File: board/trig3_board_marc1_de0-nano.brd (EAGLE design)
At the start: 233.2 x 160 mm, 305 parts, among them IC1 ICL7660CPA, IC2 ICL7660CPA, IC3 ICL7660CPA, IC4 ICL7660CPA, J10 2p-2.54, J11 2p-2.54, J12 4p-2.54, J13 BU-SMB-V, J131 4p-2.54, J14 BU-SMB-V, J141 2p-2.54, J15 2p-2.54, J16 2p-2.54, J17 2p-2.54, J18 2p-2.54, J19 6HE-160-VG64AC, J20 4p-2.54, J21 4p-2.54, J22 2p-2.54, J23 2p-2.54, J24 2p-2.54, J25 2p-2.54, J26 4p-2.54, J27 4p-2.54, J28 2p-2.54, J29 2p-2.54, J3 4p-2.54, J30 2p-2.54, J31 2p-2.54, J311 4p-2.54, J32 2p-2.54, J33 2p-2.54, J34 2p-2.54, J35 2p-2.54, J36 2p-2.54, J37 2p-2.54, J38 2p-2.54, J39 2p-2.54, J4 2p-2.54, J40 2p-2.54, J41 2p-2.54, J42 2p-2.54, J43 2p-2.54, J48 2p-2.54, J49 2p-2.54, J5 2p-2.54, J50 2p-2.54, J51 2p-2.54, J52 2p-2.54, J53 2p-2.54, J54 2p-2.54, J55 2p-2.54, J6 2p-2.54, J7 4p-2.54, J8 2p-2.54, J9 2p-2.54, K15_R10P BU-SMB-V, K16_R10N BU-SMB-V, M16CLK_3N BU-SMB-V, P11 BU-SMB-V, P14_CLKOUT_4P BU-SMB-V, P15 BU-SMB-V, P16_R15N BU-SMB-V, P9 BU-SMB-V, T10_B16N BU-SMB-V, T12_B18N BU-SMB-V, T13_B20N BU-SMB-V, T14_B23P BU-SMB-V, T15_B23N BU-SMB-V, T9CLK_7N BU-SMB-V

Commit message: slim it down and add usb-serial
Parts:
- removed A12_T21N, A14_CLKOUT_2N, A2_T2N, A3_T2P, A5, A7_T9N, A8CLK_4N, B11, B12_T21P, B16, B5, B7_T9P, B8CLK_4P, C11, C14, C15, C16, C3_CLKOUT_3N, C6, C8, C9_T15N, D11, D14, D15, D16, D3_CLKOUT_3P, D5, D6, D8, D9_T15P, E10, E11, E15CLK_2P, E16CLK_2N, E6, E7, E8_T10N, E9, F14, F15, F16, F8_T10P, F9, G15_R5P, G16_R5N, J13, J14, K15_R10P, K16_R10N, L16_R11N, M16CLK_3N, N12, N14, N15_R13P, N16_R13N, P11, P14_CLKOUT_4P, P15, R10_B16P, R12_B18P, R13_B20P, R14_CLKOUT_4N, T10_B16N, T12_B18N, T13_B20N, T14_B23P, T15_B23N: BU-SMB-V, con-coax:BU-SMB-V
- removed C1, C12, C13, C17, C18, C3, C7, C9: 10uF, SparkFun-Capacitors:CAP-PTH-5MM
- removed C19, C2, C20, C21, C22, C4, C5, C91, C93, C94, C95, C97: 0.1uF, SparkFun-Capacitors:0805
- removed IC1, IC2, IC3, IC4: ICL7660CPA, maxim:DIL08
- removed J1, J2: (no value), SparkFun-Connectors:2X13
- removed J10, J11, J141, J15, J16, J17, J18, J22, J23, J24, J25, J28, J29, J30, J31, J32, J33, J35, J36, J37, J38, J39, J4, J40, J41, J48, J49, J50, J51, J52, J53, J54, J55, J8, J9, OJ1, OJ10, OJ11, OJ12, OJ17, OJ18, OJ19, OJ2, OJ20, OJ21, OJ22, OJ23, OJ24, OJ25, OJ26, OJ27, OJ28, OJ29, OJ3, OJ30, OJ31, OJ32, OJ33, OJ34, OJ35, OJ36, OJ37, OJ38, OJ39, OJ4, OJ40, OJ49, OJ5, OJ50, OJ51, OJ52, OJ53, OJ54, OJ55, OJ56, OJ57, OJ58, OJ59, OJ6, OJ60, OJ61, OJ62, OJ63, OJ64, OJ65, OJ66, OJ67, OJ68, OJ69, OJ7, OJ70, OJ71, OJ72, OJ73, OJ74, OJ75, OJ76, OJ77, OJ78, OJ79, OJ8, OJ80, OJ9: 2p-2.54, Seeed-Connector:H2-2.54
- removed J131, J20, J21, J26, J27, J311: 4p-2.54, Seeed-Connector:H4-2.54
- removed J19: 6HE-160-VG64AC, 19inch:6HE_160-VG64AC
- removed R10, R12, R13, R14: 1k, SparkFun-Passives:AXIAL-0.3
- removed R100, R11, R111, R141, R15, R161, R18, R19, R20, R21, R22, R23, R24, R25, R26, R27, R28, R29, R30, R32, R33, R35, R39, R4, R40, R45, R46, R47, R49, R50, R51, R52, R53, R9, R91: 50, SparkFun-Passives:AXIAL-0.3
- removed R17: 10k, SparkFun-Passives:AXIAL-0.3
- removed R2, R3, R7: 3296W 5k, resistor:RTRIM3296W
- removed VSLUE, VSLUE2, VSLUE3, VSLUE4, VSLUE6, VSLUE7, VSLUE8, VSLUE9: SN74ACT244DW, SN74ACT244DW:SOIC127P1030X265-20N
- added C_OSC1, C_OSC2: 22pF, rcl@1:C0603
- added U340G: CH340G, usb-serial:SOIC16
- added USB1: MF-CON-MICROUSB-RIGHT, PP_Connectors:10118193-0001LF
- added Y1: ABL-12.000MHZ-B2, SparkFun-FreqCtrl:HC49US
- R1: value 3296W 5k -> 10k; device resistor:RTRIM3296W -> adafruit:R0805
- moved R1 126.3 mm to (95.0, 98.0)
- moved J3 110.0 mm to (-35.0, 107.0)
- moved B4 89.9 mm to (66.9, 74.0)
- moved C10 89.9 mm to (94.0, 80.0)
- moved D12 89.9 mm to (111.0, 74.0)
- moved OJ89 89.9 mm to (77.9, 68.0)
- moved OJ90 89.9 mm to (68.0, 68.0)
- moved OJ91 89.9 mm to (102.0, 68.0)
- moved OJ92 89.9 mm to (112.1, 68.0)
- moved OJ93 89.9 mm to (78.0, 64.0)
- moved OJ94 89.9 mm to (68.0, 64.0)
- moved OJ95 89.9 mm to (112.0, 64.0)
- moved OJ96 89.9 mm to (102.0, 64.0)
- moved VSLUE11 89.9 mm to (89.0, 71.0)
- moved A4 89.9 mm to (76.9, 74.0)
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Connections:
- removed net -3V3_1: C3.1, IC1.5, J20.1, R10.P$2
- removed net -3V3_2: C9.1, IC2.5, J21.1, R12.P$2
- removed net -3V3_3: C13.1, IC3.5, J26.1, R13.P$2
- removed net -3V3_4: C18.1, IC4.5, J27.1, R14.P$2
- removed net -V1: C19.2, J20.2, OJ9.1, R1.2
- removed net -V2: C20.2, J21.2, OJ10.1, R2.2
- removed net -V3: C21.2, J26.2, OJ11.1, R3.2
- removed net -V4: C22.2, J27.2, OJ12.1, R7.2
- removed net AIN0: J1.24, J131.4
- removed net AIN1: J1.25, J311.1
- removed net AIN2: J1.22, J131.3
- removed net AIN3: J1.21, J311.3
- removed net AIN4: J1.23, J311.2
- removed net AIN5: J1.18, J131.1
- removed net AIN6: J1.19, J311.4
- removed net AIN7: J1.20, J131.2
- removed net GPIO_018_E7: OJ64.1, SV1.23, VSLUE7.6, VSLUE7.8
- removed net GPIO_019_D8: OJ21.1, SV1.24, VSLUE2.15, VSLUE2.17
- removed net GPIO_01_C3: C3_CLKOUT_3N.1, J30.2, R27.P$2, SV1.4
- removed net GPIO_021_F8: F8_T10P.1, J18.2, R21.P$2, SV1.26
- removed net GPIO_022_F9: OJ62.1, SV1.27, VSLUE7.11, VSLUE7.13
- removed net GPIO_023_E9: OJ24.1, SV1.28, VSLUE2.6, VSLUE2.8
- removed net GPIO_112_N12: OJ23.1, SV2.17, VSLUE2.2, VSLUE2.4
- removed net GPIO_120_P15: OJ61.1, SV2.25, VSLUE7.15, VSLUE7.17
- removed net GPIO_20_A14: A14_CLKOUT_2N.1, J1.5, J31.2, R29.P$2
- removed net GPIO_210_F14: J1.15, OJ30.1, VSLUE3.11, VSLUE3.13
- removed net GPIO_211_G16: G16_R5N.1, J1.16, J28.2, R24.P$2
- removed net GPIO_212_G15: G15_R5P.1, J1.17, J29.2, R26.P$2
- removed net GPIO_21_B16: J1.6, OJ22.1, VSLUE2.11, VSLUE2.13
- removed net GPIO_22_C14: J1.7, OJ32.1, VSLUE3.6, VSLUE3.8
- removed net GPIO_23_C16: J1.8, OJ63.1, VSLUE7.2, VSLUE7.4
- removed net GPIO_24_C15: J1.9, OJ31.1, VSLUE3.2, VSLUE3.4
- removed net GPIO_25_D16: J1.10, OJ39.1, VSLUE4.2, VSLUE4.4
- removed net GPIO_26_D15: J1.11, OJ29.1, VSLUE3.15, VSLUE3.17
- removed net GPIO_27_D14: J1.12, OJ40.1, VSLUE4.6, VSLUE4.8
- removed net GPIO_28_F15: J1.13, OJ37.1, VSLUE4.15, VSLUE4.17
- removed net GPIO_29_F16: J1.14, OJ38.1, VSLUE4.11, VSLUE4.13
- removed net GPIO_2_IN0_E15CLK: E15CLK_2P.1, J1.2, J16.2, R19.P$2
- removed net GPIO_2_IN1_E16CLK: E16CLK_2N.1, J1.3, J15.2, R18.P$2
- removed net GPIO_2_IN2_M16CLK: J1.4, J141.2, M16CLK_3N.1, R15.P$2
- removed net N$1: C1.1, IC1.2
- removed net N$10: R1.3, R10.P$1
- removed net N$11: R12.P$1, R2.3
- removed net N$12: R13.P$1, R3.3
- removed net N$13: R14.P$1, R7.3
- removed net N$2: C1.2, IC1.4
- removed net N$3: C12.1, IC3.2
- removed net N$4: C7.1, IC2.2
- removed net N$5: C7.2, IC2.4
- removed net N$6: C12.2, IC3.4
- removed net N$7: C17.1, IC4.2
- removed net N$8: C17.2, IC4.4
- removed net OUT1: J14.1, OJ1.1, VSLUE.16, VSLUE.18
- removed net OUT10: E9.1, OJ19.1, VSLUE2.12, VSLUE2.14
- removed net OUT11: D8.1, OJ17.1, VSLUE2.3, VSLUE2.5
- removed net OUT12: B16.1, OJ18.1, VSLUE2.7, VSLUE2.9
- removed net OUT13: C15.1, OJ28.1, VSLUE3.16, VSLUE3.18
- removed net OUT14: C14.1, OJ27.1, VSLUE3.12, VSLUE3.14
- removed net OUT15: D15.1, OJ25.1, VSLUE3.3, VSLUE3.5
- removed net OUT16: F14.1, OJ26.1, VSLUE3.7, VSLUE3.9
- removed net OUT17: D16.1, OJ36.1, VSLUE4.16, VSLUE4.18
- removed net OUT18: D14.1, OJ35.1, VSLUE4.12, VSLUE4.14
- removed net OUT19: F15.1, OJ33.1, VSLUE4.3, VSLUE4.5
- removed net OUT2: D11.1, OJ2.1, VSLUE.12, VSLUE.14
- removed net OUT20: F16.1, OJ34.1, VSLUE4.7, VSLUE4.9
- removed net OUT25: D6.1, OJ52.1, VSLUE6.16, VSLUE6.18
- removed net OUT26: C6.1, OJ51.1, VSLUE6.12, VSLUE6.14
- removed net OUT27: C8.1, OJ49.1, VSLUE6.3, VSLUE6.5
- removed net OUT28: E6.1, OJ50.1, VSLUE6.7, VSLUE6.9
- removed net OUT29: C16.1, OJ60.1, VSLUE7.16, VSLUE7.18
- removed net OUT3: B11.1, OJ3.1, VSLUE.7, VSLUE.9
- removed net OUT30: E7.1, OJ59.1, VSLUE7.12, VSLUE7.14
- removed net OUT31: OJ57.1, P15.1, VSLUE7.3, VSLUE7.5
- removed net OUT32: F9.1, OJ58.1, VSLUE7.7, VSLUE7.9
- removed net OUT33: B5.1, OJ68.1, VSLUE8.16, VSLUE8.18
- removed net OUT34: A5.1, OJ67.1, VSLUE8.12, VSLUE8.14
- removed net OUT35: D5.1, OJ65.1, VSLUE8.3, VSLUE8.5
- removed net OUT36: N14.1, OJ66.1, VSLUE8.7, VSLUE8.9
- removed net OUT37: E11.1, OJ76.1, VSLUE9.16, VSLUE9.18
- removed net OUT38: OJ75.1, P11.1, VSLUE9.12, VSLUE9.14
- removed net OUT39: J13.1, OJ73.1, VSLUE9.3, VSLUE9.5
- removed net OUT4: E10.1, OJ4.1, VSLUE.3, VSLUE.5
- removed net OUT40: C11.1, OJ74.1, VSLUE9.7, VSLUE9.9
- removed net OUT9: N12.1, OJ20.1, VSLUE2.16, VSLUE2.18
- new net +3V3: U340G.16, U340G.4
- new net DMINUS: U340G.6, USB1.2
- new net DPLUS: U340G.5, USB1.3
- new net N$23: C_OSC1.1, U340G.7, Y1.1
- new net N$31: C_OSC2.1, U340G.8, Y1.2
- new net SLD: USB1.S1, USB1.S2, USB1.S3, USB1.S4
- net 3V3: no longer IC1.8, IC2.8, IC3.8, IC4.8, J1.1, J20.4, J21.4, J26.4, J27.4
- net 5V: now also R1.2, USB1.1; no longer C2.2, C4.2, C5.2, C91.2, C93.2, C94.2, C95.2, C97.2, J19.1-A32, J19.1-C32, J19.2-A32, J19.2-C32, R17.P$1, VSLUE.20, VSLUE2.20, VSLUE3.20, VSLUE4.20, VSLUE6.20, VSLUE7.20, VSLUE8.20, VSLUE9.20
- net GND: now also C_OSC1.2, C_OSC2.2, U340G.1, USB1.5; no longer A12_T21N.2, A12_T21N.3, A12_T21N.4, A12_T21N.5, A14_CLKOUT_2N.2, A14_CLKOUT_2N.3, A14_CLKOUT_2N.4, A14_CLKOUT_2N.5, A2_T2N.2, A2_T2N.3, A2_T2N.4, A2_T2N.5, A3_T2P.2, A3_T2P.3, A3_T2P.4, A3_T2P.5, A5.2, A5.3, A5.4, A5.5, A7_T9N.2, A7_T9N.3, A7_T9N.4, A7_T9N.5, A8CLK_4N.2, A8CLK_4N.3, A8CLK_4N.4, A8CLK_4N.5, B11.2, B11.3, B11.4, B11.5, B12_T21P.2, B12_T21P.3, B12_T21P.4, B12_T21P.5, B16.2, B16.3, B16.4, B16.5, B5.2, B5.3, B5.4, B5.5, B7_T9P.2, B7_T9P.3, B7_T9P.4, B7_T9P.5, B8CLK_4P.2, B8CLK_4P.3, B8CLK_4P.4, B8CLK_4P.5, C11.2, C11.3, C11.4, C11.5, C13.2, C14.2, C14.3, C14.4, C14.5, C15.2, C15.3, C15.4, C15.5, C16.2, C16.3, C16.4, C16.5, C18.2, C19.1, C2.1, C20.1, C21.1, C22.1, C3.2, C3_CLKOUT_3N.2, C3_CLKOUT_3N.3, C3_CLKOUT_3N.4, C3_CLKOUT_3N.5, C4.1, C5.1, C6.2, C6.3, C6.4, C6.5, C8.2, C8.3, C8.4, C8.5, C9.2, C91.1, C93.1, C94.1, C95.1, C97.1, C9_T15N.2, C9_T15N.3, C9_T15N.4, C9_T15N.5, D11.2, D11.3, D11.4, D11.5, D14.2, D14.3, D14.4, D14.5, D15.2, D15.3, D15.4, D15.5, D16.2, D16.3, D16.4, D16.5, D3_CLKOUT_3P.2, D3_CLKOUT_3P.3, D3_CLKOUT_3P.4, D3_CLKOUT_3P.5, D5.2, D5.3, D5.4, D5.5, D6.2, D6.3, D6.4, D6.5, D8.2, D8.3, D8.4, D8.5, D9_T15P.2, D9_T15P.3, D9_T15P.4, D9_T15P.5, E10.2, E10.3, E10.4, E10.5, E11.2, E11.3, E11.4, E11.5, E15CLK_2P.2, E15CLK_2P.3, E15CLK_2P.4, E15CLK_2P.5, E16CLK_2N.2, E16CLK_2N.3, E16CLK_2N.4, E16CLK_2N.5, E6.2, E6.3, E6.4, E6.5, E7.2, E7.3, E7.4, E7.5, E8_T10N.2, E8_T10N.3, E8_T10N.4, E8_T10N.5, E9.2, E9.3, E9.4, E9.5, F14.2, F14.3, F14.4, F14.5, F15.2, F15.3, F15.4, F15.5, F16.2, F16.3, F16.4, F16.5, F8_T10P.2, F8_T10P.3, F8_T10P.4, F8_T10P.5, F9.2, F9.3, F9.4, F9.5, G15_R5P.2, G15_R5P.3, G15_R5P.4, G15_R5P.5, G16_R5N.2, G16_R5N.3, G16_R5N.4, G16_R5N.5, IC1.3, IC2.3, IC3.3, IC4.3, J1.26, J10.1, J11.1, J13.2, J13.3, J13.4, J13.5, J14.2, J14.3, J14.4, J14.5, J141.1, J15.1, J16.1, J17.1, J18.1, J19.1-A9, J19.1-C9, J19.2-A9, J19.2-C9, J20.3, J21.3, J22.1, J23.1, J24.1, J25.1, J26.3, J27.3, J28.1, J29.1, J30.1, J31.1, J32.1, J33.1, J35.1, J36.1, J37.1, J38.1, J39.1, J4.1, J40.1, J41.1, J48.1, J49.1, J50.1, J51.1, J52.1, J53.1, J54.1, J55.1, J8.1, J9.1, K15_R10P.2, K15_R10P.3, K15_R10P.4, K15_R10P.5, K16_R10N.2, K16_R10N.3, K16_R10N.4, K16_R10N.5, L16_R11N.2, L16_R11N.3, L16_R11N.4, L16_R11N.5, M16CLK_3N.2, M16CLK_3N.3, M16CLK_3N.4, M16CLK_3N.5, N12.2, N12.3, N12.4, N12.5, N14.2, N14.3, N14.4, N14.5, N15_R13P.2, N15_R13P.3, N15_R13P.4, N15_R13P.5, N16_R13N.2, N16_R13N.3, N16_R13N.4, N16_R13N.5, OJ1.2, OJ17.2, OJ18.2, OJ19.2, OJ2.2, OJ20.2, OJ21.2, OJ22.2, OJ23.2, OJ24.2, OJ25.2, OJ26.2, OJ27.2, OJ28.2, OJ29.2, OJ3.2, OJ30.2, OJ31.2, OJ32.2, OJ33.2, OJ34.2, OJ35.2, OJ36.2, OJ37.2, OJ38.2, OJ39.2, OJ4.2, OJ40.2, OJ49.2, OJ5.2, OJ50.2, OJ51.2, OJ52.2, OJ53.2, OJ54.2, OJ55.2, OJ56.2, OJ57.2, OJ58.2, OJ59.2, OJ6.2, OJ60.2, OJ61.2, OJ62.2, OJ63.2, OJ64.2, OJ65.2, OJ66.2, OJ67.2, OJ68.2, OJ69.2, OJ7.2, OJ70.2, OJ71.2, OJ72.2, OJ73.2, OJ74.2, OJ75.2, OJ76.2, OJ77.2, OJ78.2, OJ79.2, OJ8.2, OJ80.2, P11.2, P11.3, P11.4, P11.5, P14_CLKOUT_4P.2, P14_CLKOUT_4P.3, P14_CLKOUT_4P.4, P14_CLKOUT_4P.5, P15.2, P15.3, P15.4, P15.5, R1.1, R100.P$1, R10_B16P.2, R10_B16P.3, R10_B16P.4, R10_B16P.5, R11.P$1, R111.P$1, R12_B18P.2, R12_B18P.3, R12_B18P.4, R12_B18P.5, R13_B20P.2, R13_B20P.3, R13_B20P.4, R13_B20P.5, R141.P$1, R14_CLKOUT_4N.2, R14_CLKOUT_4N.3, R14_CLKOUT_4N.4, R14_CLKOUT_4N.5, R15.P$1, R161.P$1, R18.P$1, R19.P$1, R2.1, R20.P$1, R21.P$1, R22.P$1, R23.P$1, R24.P$1, R25.P$1, R26.P$1, R27.P$1, R28.P$1, R29.P$1, R3.1, R30.P$1, R32.P$1, R33.P$1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
- net GPIO_00_D3: no longer D3_CLKOUT_3P.1, J50.2, R51.P$2
- net GPIO_012_B7: no longer B7_T9P.1, J49.2, R50.P$2
- net GPIO_013_D6: no longer OJ55.1, VSLUE6.2, VSLUE6.4
- net GPIO_014_A7: no longer A7_T9N.1, J35.2, OJ9.2, R33.P$2
- net GPIO_015_C6: no longer OJ56.1, VSLUE6.6, VSLUE6.8
- net GPIO_016_C8: no longer OJ53.1, VSLUE6.15, VSLUE6.17
- net GPIO_017_E6: no longer OJ54.1, VSLUE6.11, VSLUE6.13
- net GPIO_020_E8: no longer E8_T10N.1, J41.2, OJ12.2, R40.P$2
- net GPIO_024_C9: no longer C9_T15N.1, J8.2, R91.P$2
- net GPIO_025_D9: no longer D9_T15P.1, J11.2, R141.P$2
- net GPIO_026_E11: no longer OJ79.1, VSLUE9.2, VSLUE9.4
- net GPIO_027_E10: no longer OJ5.1, VSLUE.15, VSLUE.17
- net GPIO_028_C11: no longer OJ78.1, VSLUE9.11, VSLUE9.13
- net GPIO_029_B11: no longer OJ6.1, VSLUE.11, VSLUE.13
- net GPIO_02_A2: no longer A2_T2N.1, J22.2, R20.P$2
- net GPIO_030_A12: no longer A12_T21N.1, J36.2, OJ10.2, R9.P$2
- net GPIO_031_D11: no longer OJ8.1, VSLUE.6, VSLUE.8
- net GPIO_033_B12: no longer B12_T21P.1, J37.2, R11.P$2
- net GPIO_03_A3: no longer A3_T2P.1, J25.2, R25.P$2
- net GPIO_07_B5: no longer OJ71.1, VSLUE8.2, VSLUE8.4
- net GPIO_08_A5: no longer OJ72.1, VSLUE8.6, VSLUE8.8
- net GPIO_09_D5: no longer OJ69.1, VSLUE8.15, VSLUE8.17
- net GPIO_0_IN0_A8CLK: no longer A8CLK_4N.1, J24.2, R23.P$2
- net GPIO_0_IN1_B8CLK: no longer B8CLK_4P.1, J23.2, R22.P$2
- net GPIO_110_P11: no longer OJ80.1, VSLUE9.6, VSLUE9.8
- net GPIO_111_R10: no longer J48.2, R10_B16P.1, R49.P$2
- net GPIO_114_N9: now also R1.1; no longer R17.P$2, VSLUE.1, VSLUE.19, VSLUE2.1, VSLUE2.19, VSLUE3.1, VSLUE3.19, VSLUE4.1, VSLUE4.19, VSLUE6.1, VSLUE6.19, VSLUE7.1, VSLUE7.19, VSLUE8.1, VSLUE8.19, VSLUE9.1, VSLUE9.19
- net GPIO_116_L16: no longer J32.2, L16_R11N.1, R28.P$2
- net GPIO_117_K16: no longer J33.2, K16_R10N.1, R30.P$2
- net GPIO_11_T15: no longer J40.2, OJ11.2, R39.P$2, T15_B23N.1
- net GPIO_122_R14: no longer J53.2, R14_CLKOUT_4N.1, R46.P$2
- net GPIO_123_N16: no longer J55.2, N16_R13N.1, R52.P$2
- net GPIO_124_N15: no longer J54.2, N15_R13P.1, R47.P$2
- net GPIO_125_P14: no longer J52.2, P14_CLKOUT_4P.1, R45.P$2
- net GPIO_126_L14: now also U340G.3
- net GPIO_127_N14: no longer OJ70.1, VSLUE8.11, VSLUE8.13
- net GPIO_129_L13: now also U340G.2
- net GPIO_12_T14: no longer J4.2, R4.P$2, T14_B23P.1
- net GPIO_131_K15: no longer J39.2, K15_R10P.1, R35.P$2
- net GPIO_132_J13: no longer OJ77.1, VSLUE9.15, VSLUE9.17
- net GPIO_133_J14: no longer OJ7.1, VSLUE.2, VSLUE.4
- net GPIO_13_T13: no longer J38.2, R32.P$2, T13_B20N.1
- net GPIO_14_R13: no longer J17.2, R13_B20P.1, R161.P$2
- net GPIO_15_T12: no longer J9.2, R100.P$2, T12_B18N.1
- net GPIO_16_R12: no longer J10.2, R111.P$2, R12_B18P.1
- net GPIO_18_T10: no longer J51.2, R53.P$2, T10_B16N.1
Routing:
- net GPIO_114_N9: track 0.00 -> 219.5 mm, vias 0 -> 1
- net GPIO_113_P9: track 0.00 -> 109.4 mm, vias 0 -> 1
- net GPIO_115_N11: track 0.00 -> 109.0 mm
- net 3V3: track 0.00 -> 96.5 mm
- net GPIO_126_L14: track 0.00 -> 89.9 mm, vias 0 -> 1
- net GPIO_010_B6: track 0.00 -> 86.6 mm, vias 0 -> 1
- net GPIO_032_D12: track 0.00 -> 84.3 mm, vias 0 -> 1
- net GPIO_129_L13: track 0.00 -> 83.4 mm, vias 0 -> 1
- net GPIO_19_R11: track 0.00 -> 82.3 mm
- net GPIO_04_B3: track 0.00 -> 78.9 mm, vias 0 -> 1
- net GPIO_011_A6: track 0.00 -> 75.1 mm, vias 0 -> 1
- net GPIO_05_B4: track 0.00 -> 72.5 mm, vias 0 -> 1
- net GPIO_06_A4: track 0.00 -> 68.7 mm, vias 0 -> 1
- net GPIO_10_F13: track 0.00 -> 68.6 mm
- net GPIO_119_L15: track 0.00 -> 60.6 mm
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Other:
- board size 233.2 x 160 mm -> 173 x 72 mm
- board text removed: "-3v3_1"
- board text removed: "-3v3_2"
- board text removed: "-3v3_3"
- board text removed: "-3v3_4"
- board text removed: "-V1"
- board text removed: "-V2"
- board text removed: "-V3"
- board text removed: "-V4"
- board text removed: "AIN0"
- board text removed: "AIN1"
- board text removed: "AIN2"
- board text removed: "AIN3"
- board text removed: "AIN4"
- board text removed: "AIN5"
- board text removed: "AIN6"
- board text removed: "AIN7"
- board text removed: "de0-nano_2x13 board"
- board text removed: "optional negative voltage references"

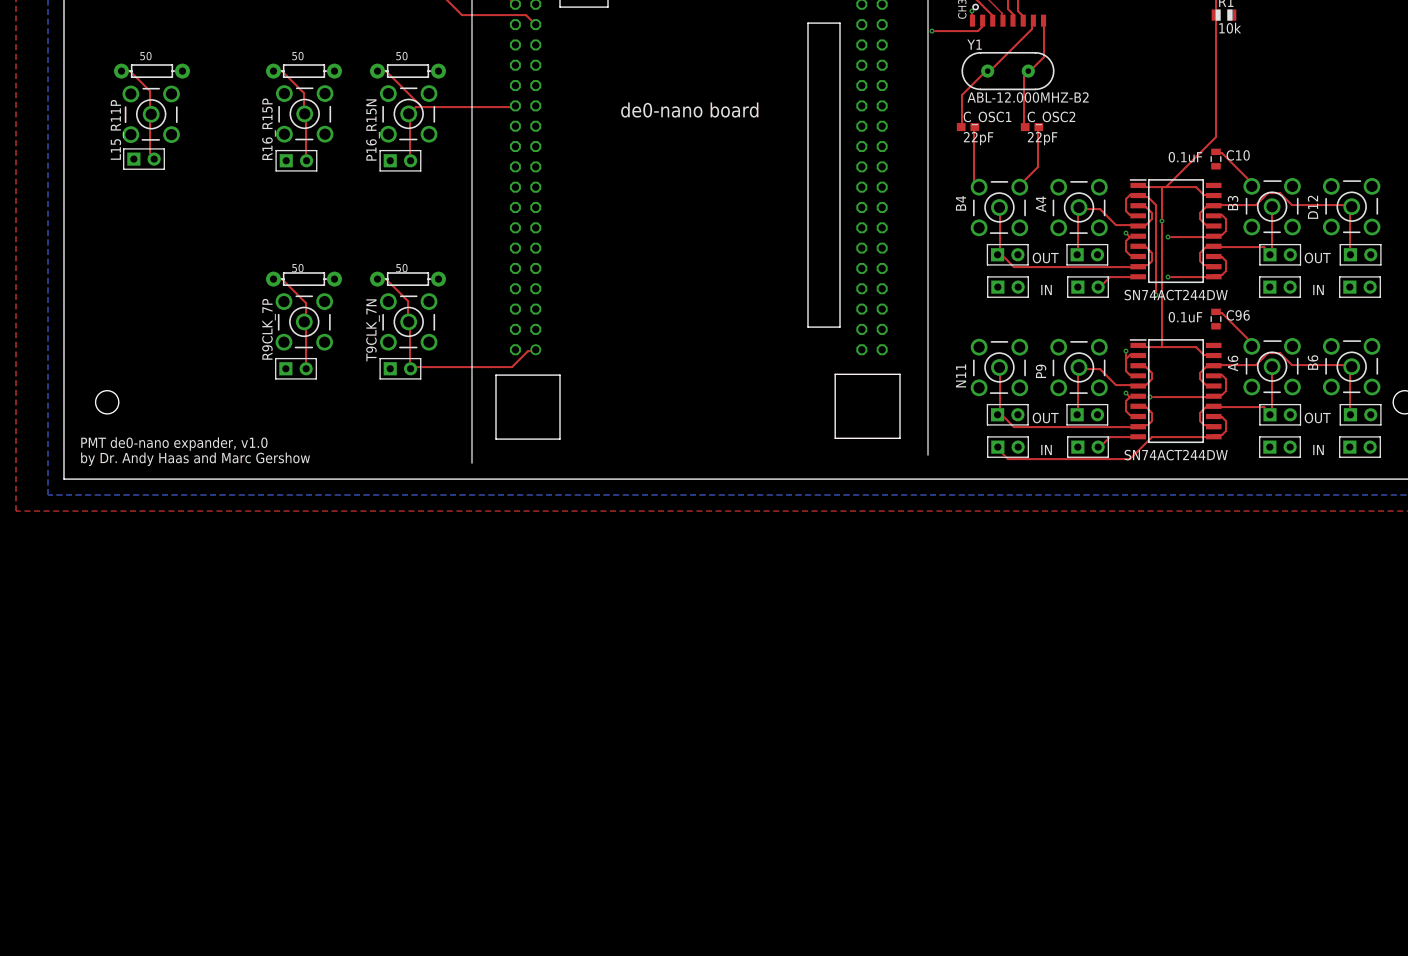
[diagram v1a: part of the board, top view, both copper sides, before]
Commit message: updated board schematics: input circuit redesign
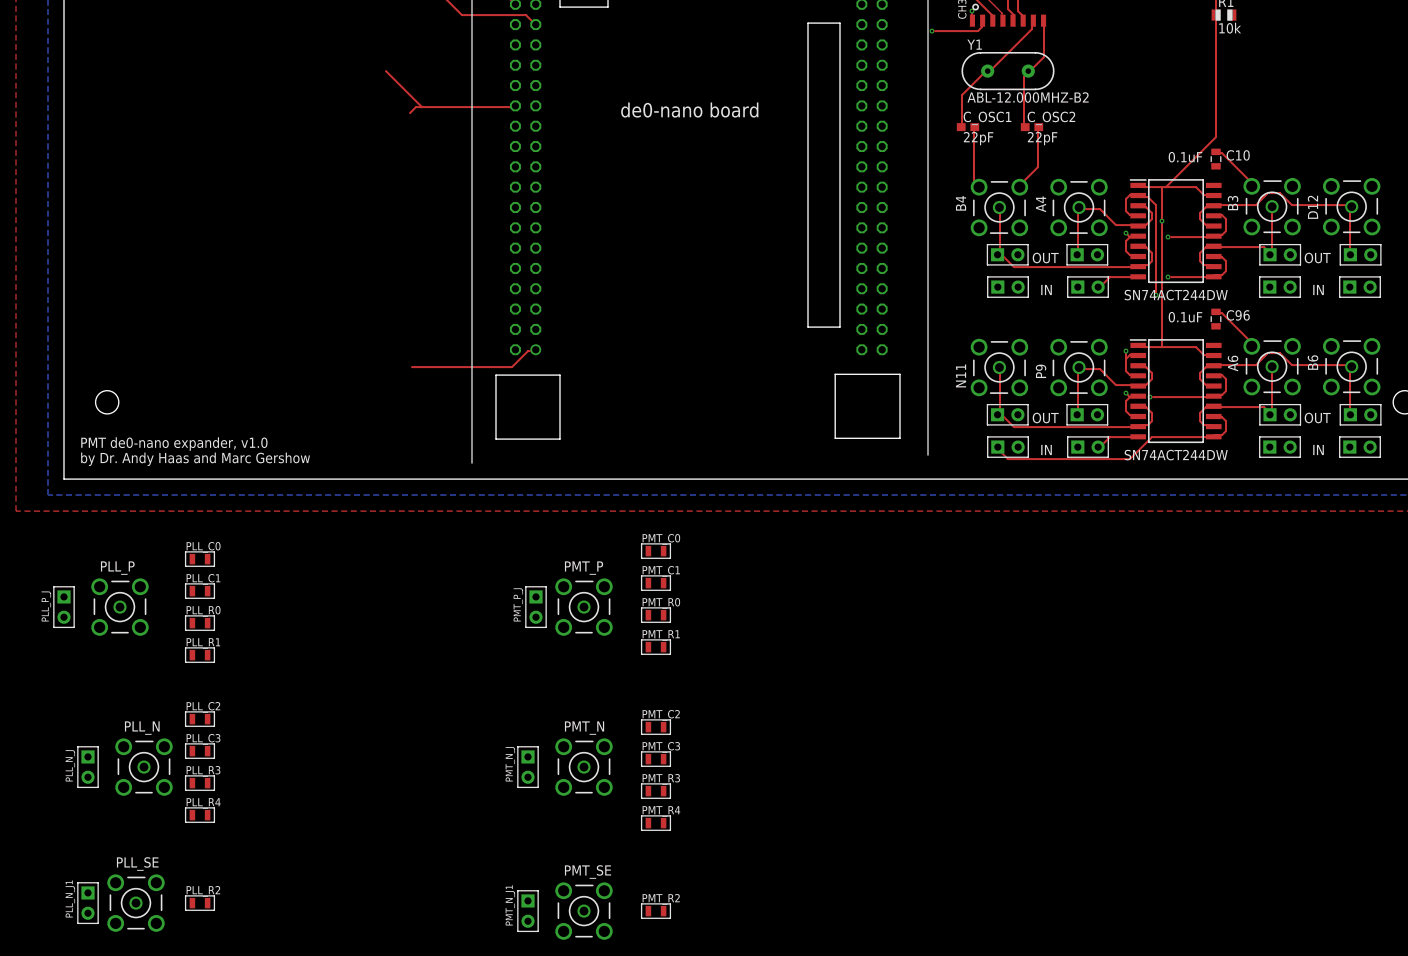
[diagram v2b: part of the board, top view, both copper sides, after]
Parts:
- removed J34, J42, J43, J5, J6: 2p-2.54, Seeed-Connector:H2-2.54
- removed L15_R11P, P16_R15N, R16_R15P, R9CLK_7P, T9CLK_7N: BU-SMB-V, con-coax:BU-SMB-V
- removed R31, R41, R43, R5, R6: 50, SparkFun-Passives:AXIAL-0.3
- added PLL_C0, PLL_C2, PMT_C0, PMT_C2: 1uF, MF_Passives:C0805
- added PLL_C1, PMT_C1: 0.1uF, MF_Passives:C0805
- added PLL_C3, PMT_C3: (no value), MF_Passives:C0805
- added PLL_N, PLL_P, PLL_SE, PMT_N, PMT_P, PMT_SE: BU-SMB-V, con-coax:BU-SMB-V
- added PLL_N_J, PLL_N_J1, PLL_P_J, PMT_N_J, PMT_N_J1, PMT_P_J: 2p-2.54, Seeed-Connector:H2-2.54
- added PLL_R0, PLL_R1, PLL_R3, PLL_R4, PMT_R0, PMT_R1, PMT_R3, PMT_R4: (no value), MF_Passives:R0805
- added PLL_R2, PMT_R2: 50ohm, MF_Passives:R0805
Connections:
- new net N$14: PLL_C0.P$1, PLL_P.1, PLL_P_J.2
- new net N$19: PLL_C2.P$1, PLL_N.1, PLL_N_J.2
- new net N$2: PMT_C0.P$1, PMT_P.1, PMT_P_J.2
- new net N$8: PMT_C2.P$1, PMT_N.1, PMT_N_J.2
- net 3V3: now also PMT_C1.P$1, PMT_C3.P$1, PMT_R0.P$1, PMT_R3.P$1
- net 5V: now also PLL_C1.P$1, PLL_C3.P$1, PLL_R0.P$1, PLL_R3.P$1
- net GND: now also PLL_C1.P$2, PLL_C3.P$2, PLL_N.2, PLL_N.3, PLL_N.4, PLL_N.5, PLL_N_J.1, PLL_N_J1.1, PLL_P.2, PLL_P.3, PLL_P.4, PLL_P.5, PLL_P_J.1, PLL_R1.P$2, PLL_R2.P$2, PLL_R4.P$2, PLL_SE.2, PLL_SE.3, PLL_SE.4, PLL_SE.5, PMT_C1.P$2, PMT_C3.P$2, PMT_N.2, PMT_N.3, PMT_N.4, PMT_N.5, PMT_N_J.1, PMT_N_J1.1, PMT_P.2, PMT_P.3, PMT_P.4, PMT_P.5, PMT_P_J.1, PMT_R1.P$2, PMT_R2.P$2, PMT_R4.P$2, PMT_SE.2, PMT_SE.3, PMT_SE.4, PMT_SE.5; no longer J34.1, J42.1, J43.1, J5.1, J6.1, L15_R11P.2, L15_R11P.3, L15_R11P.4, L15_R11P.5, P16_R15N.2, P16_R15N.3, P16_R15N.4, P16_R15N.5, R16_R15P.2, R16_R15P.3, R16_R15P.4, R16_R15P.5, R31.P$1, R41.P$1, R43.P$1, R5.P$1, R6.P$1, R9CLK_7P.2, R9CLK_7P.3, R9CLK_7P.4, R9CLK_7P.5, T9CLK_7N.2, T9CLK_7N.3, T9CLK_7N.4, T9CLK_7N.5
- net GPIO_0_IN0_A8CLK: now also PLL_C2.P$2, PLL_R3.P$2, PLL_R4.P$1
- net GPIO_0_IN1_B8CLK: now also PLL_C0.P$2, PLL_R0.P$2, PLL_R1.P$1
- net GPIO_118_R16: now also PMT_C0.P$2, PMT_R0.P$2, PMT_R1.P$1; no longer J34.2, R16_R15P.1, R31.P$2
- net GPIO_119_L15: now also PMT_N_J1.2, PMT_R2.P$1, PMT_SE.1; no longer J43.2, L15_R11P.1, R43.P$2
- net GPIO_121_P16: now also PMT_C2.P$2, PMT_R3.P$2, PMT_R4.P$1; no longer J42.2, P16_R15N.1, R41.P$2
- net GPIO_1_IN0_T9CLK: no longer J6.2, R6.P$2, T9CLK_7N.1
- net GPIO_1_IN1_R9CLK: now also PLL_N_J1.2, PLL_R2.P$1, PLL_SE.1; no longer J5.2, R5.P$2, R9CLK_7P.1
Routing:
- net GPIO_1_IN1_R9CLK: track 45.3 -> 31.3 mm
- net GPIO_119_L15: track 60.6 -> 46.6 mm
- net GPIO_1_IN0_T9CLK: track 30.2 -> 16.4 mm
- net GPIO_118_R16: track 44.0 -> 30.2 mm
- net GPIO_121_P16: track 27.1 -> 19.9 mm
